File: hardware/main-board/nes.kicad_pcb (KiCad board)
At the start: 2 copper layers, 127 x 114.3 mm, 137 parts, among them J1 Power Jack, J2 Input Board, J3 Speaker, J4 Program, J5 NHD OLED Connector, J6 microSD Socket, Q1 S8050, Q2 S8050, Q3 S8050, SW1 NES Reset, SW2 ESP Reset, U1 R-78E5.0-0.5, U10 74HCT00, U11 PCA9564, U12 MCP7940N, U13 ESP-WROOM-32, U15 EClamp2410P, U2 R-78E3.3-0.5, U3 74LVC1404, U4 RP2A03, U5 74HCT138, U6 LM4889, U7 AS6C6264, U8 MCP40D17, U9 AT28C64B, Y1 21.5 MHz, Y2 32.768 kHz

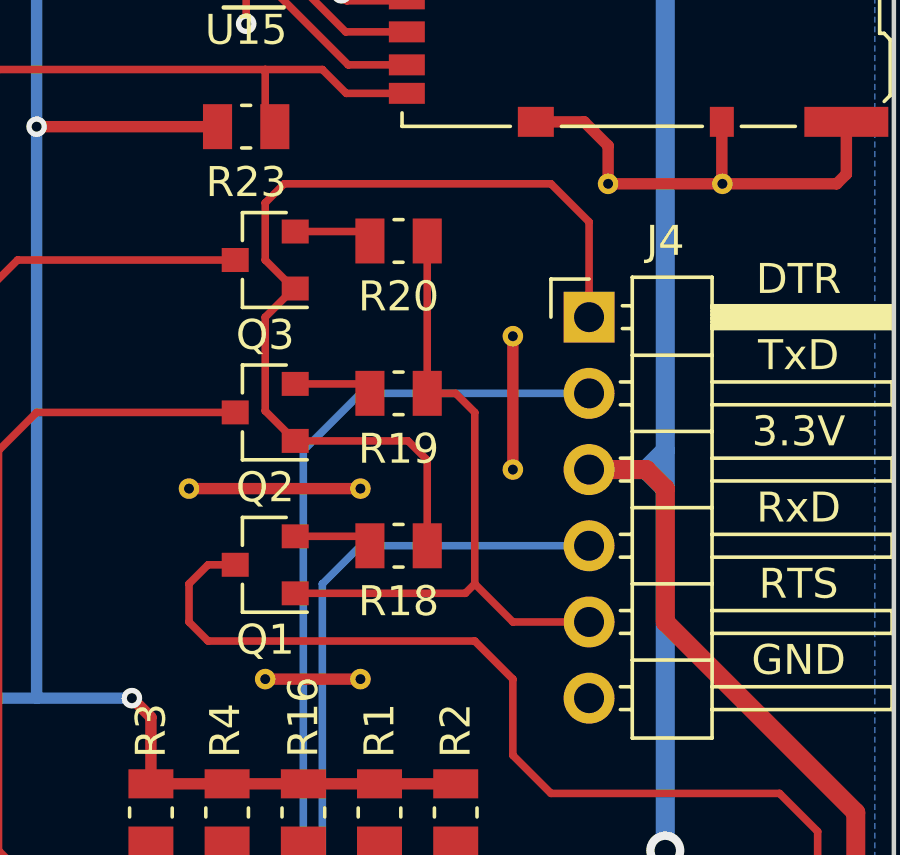
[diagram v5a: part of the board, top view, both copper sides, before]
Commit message: Create new component to fix Q1/Q2/Q3 pin mapping issues
Apparently the S8050 included in the KiCad library was for the TO-92
version of the part, for which the pin mapping was correct. The part
we're using is a SOT-23, more completely called SS8050, and has
different specifications. So fixing the issue meant creating a new
library symbol with the right pin assignments.

The PCB layout has also been updated to reflect this change.

Fixes #5
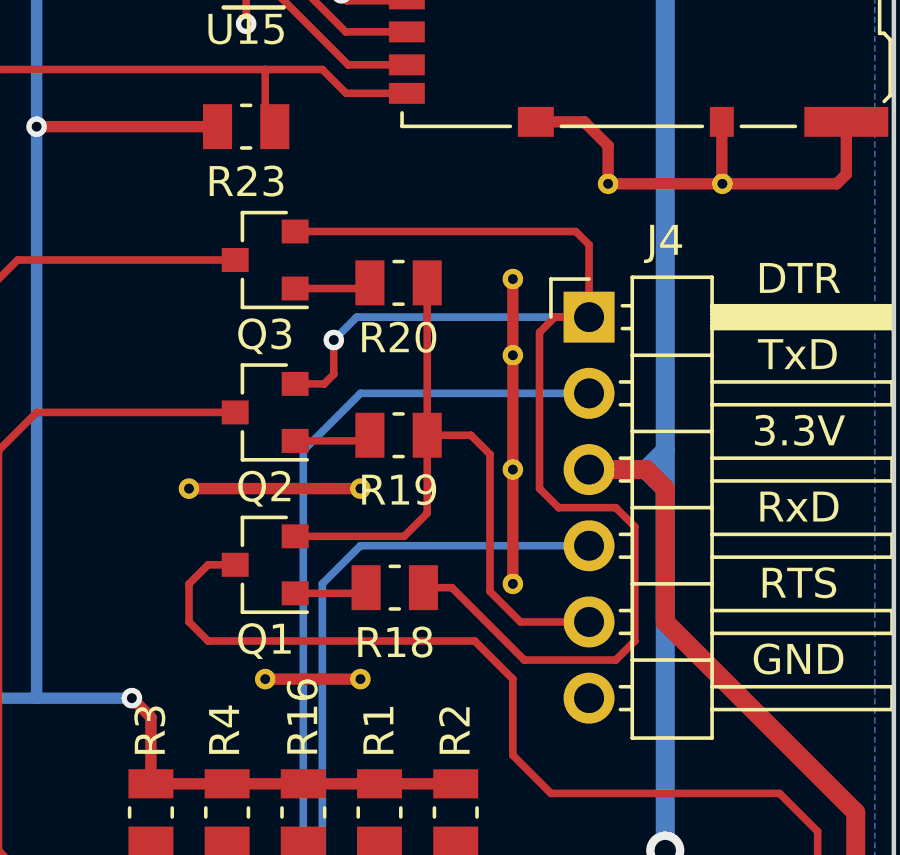
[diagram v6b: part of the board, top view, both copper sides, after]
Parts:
- added REF**: Via_27mill, lib_fp:Via_27mill, F.Cu at (174.0, 104.8)
- added REF**: Via_27mill, lib_fp:Via_27mill, F.Cu at (174.0, 97.2)
- Q1, Q2, Q3: value S8050 -> SS8050
- moved REF** 1.91 mm to (174.0, 94.6)
- moved R18 1.40 mm to (170.1, 104.9)
- moved R19 1.40 mm to (170.2, 99.8)
- moved R20 1.40 mm to (170.2, 94.7)
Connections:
- Q1 pad 1: /ESP32 Microcontroller/RTS -> Net-(Q1-Pad1)
- Q1 pad 2: Net-(Q1-Pad2) -> /ESP32 Microcontroller/RTS
- Q2 pad 1: /ESP32 Microcontroller/DTR -> Net-(Q2-Pad1)
- Q2 pad 2: Net-(Q2-Pad2) -> /ESP32 Microcontroller/DTR
- Q3 pad 1: /ESP32 Microcontroller/DTR -> Net-(Q3-Pad1)
- Q3 pad 2: Net-(Q3-Pad2) -> /ESP32 Microcontroller/DTR
- R18 pad 2: Net-(Q1-Pad2) -> Net-(Q1-Pad1)
- R19 pad 2: Net-(Q2-Pad2) -> Net-(Q2-Pad1)
- R20 pad 2: Net-(Q3-Pad2) -> Net-(Q3-Pad1)
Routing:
- net /ESP32 Microcontroller/DTR: track 31.8 -> 46.7 mm, vias 0 -> 1
- net GND: track 414.5 -> 420.3 mm
- net Net-(Q3-Pad1): track 0.00 -> 2.66 mm
- net Net-(Q3-Pad2): track 2.62 -> 0.00 mm
- net Net-(Q2-Pad2): track 2.62 -> 0.00 mm
- net Net-(Q1-Pad2): track 2.62 -> 0.00 mm
- net Net-(Q2-Pad1): track 0.00 -> 2.57 mm
- net Net-(Q1-Pad1): track 0.00 -> 2.44 mm

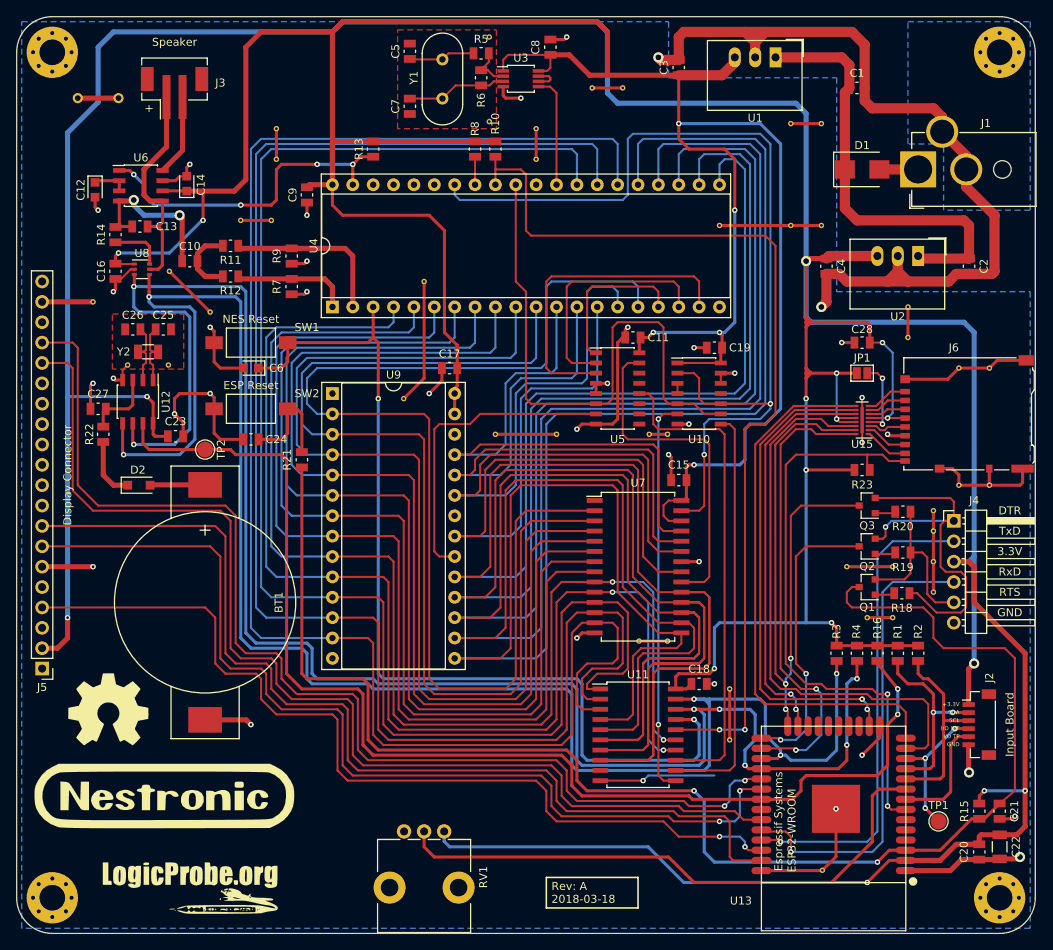
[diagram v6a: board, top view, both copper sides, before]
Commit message: Swap U11 from SOIC to TSSOP footprint
This was a trivial part change, with quite extensive trace routing
changes.

Fixes #2
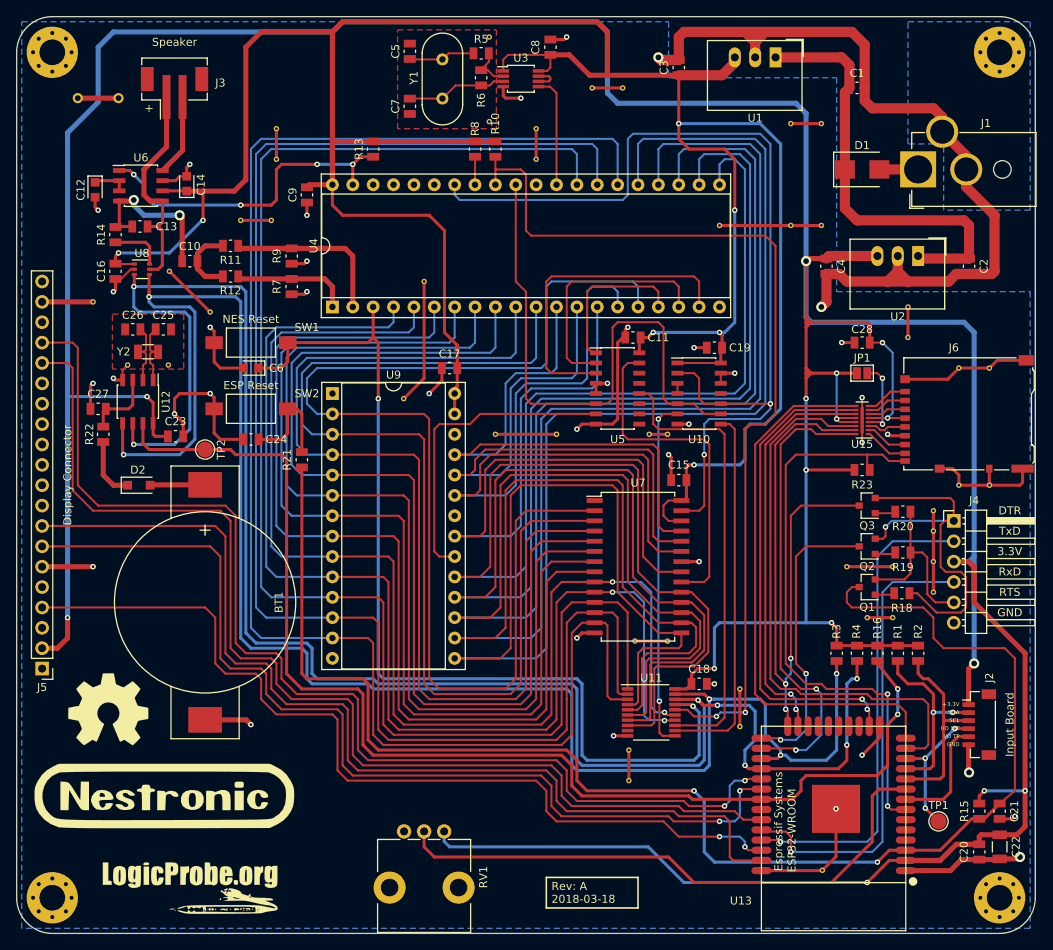
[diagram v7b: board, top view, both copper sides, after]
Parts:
- added REF**: Via_27mill, lib_fp:Via_27mill, F.Cu at (136.0, 124.5)
- added REF**: Via_27mill, lib_fp:Via_27mill, F.Cu at (136.0, 128.3)
- U11: footprint Package_SO:SOIC-20W_7.5x12.8mm_P1.27mm -> Package_SO:TSSOP-20_4.4x6.5mm_P0.65mm
- moved U11 3.25 mm to (138.8, 119.8)
- moved REF** 2.08 mm to (149.9, 121.5)
- moved REF** 1.27 mm to (149.9, 116.8)
- moved REF** 0.51 mm to (136.8, 110.9)
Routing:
- net /NES CPU/D7: track 219.8 -> 173.4 mm
- net /NES CPU/D6: track 222.0 -> 180.7 mm
- net /NES CPU/D5: track 224.2 -> 188.0 mm
- net GND: track 420.3 -> 410.2 mm
- net /NES CPU/D2: track 200.4 -> 194.6 mm
- net /NES CPU/~WR: track 49.5 -> 44.0 mm
- net /NES CPU/D1: track 195.4 -> 190.0 mm
- net /NES CPU/~RD: track 51.5 -> 46.5 mm
- net /NES CPU/D0: track 190.3 -> 185.3 mm
- net /NES CPU/D3: track 204.1 -> 199.4 mm
- net /NES CPU/D4: track 200.5 -> 196.0 mm
- net /NES CPU/Y3: track 61.0 -> 56.5 mm
- net /NES CPU/A0: track 150.5 -> 147.1 mm
- net /NES CPU/A1: track 151.8 -> 148.8 mm
- net +3V3: track 569.4 -> 566.9 mm
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
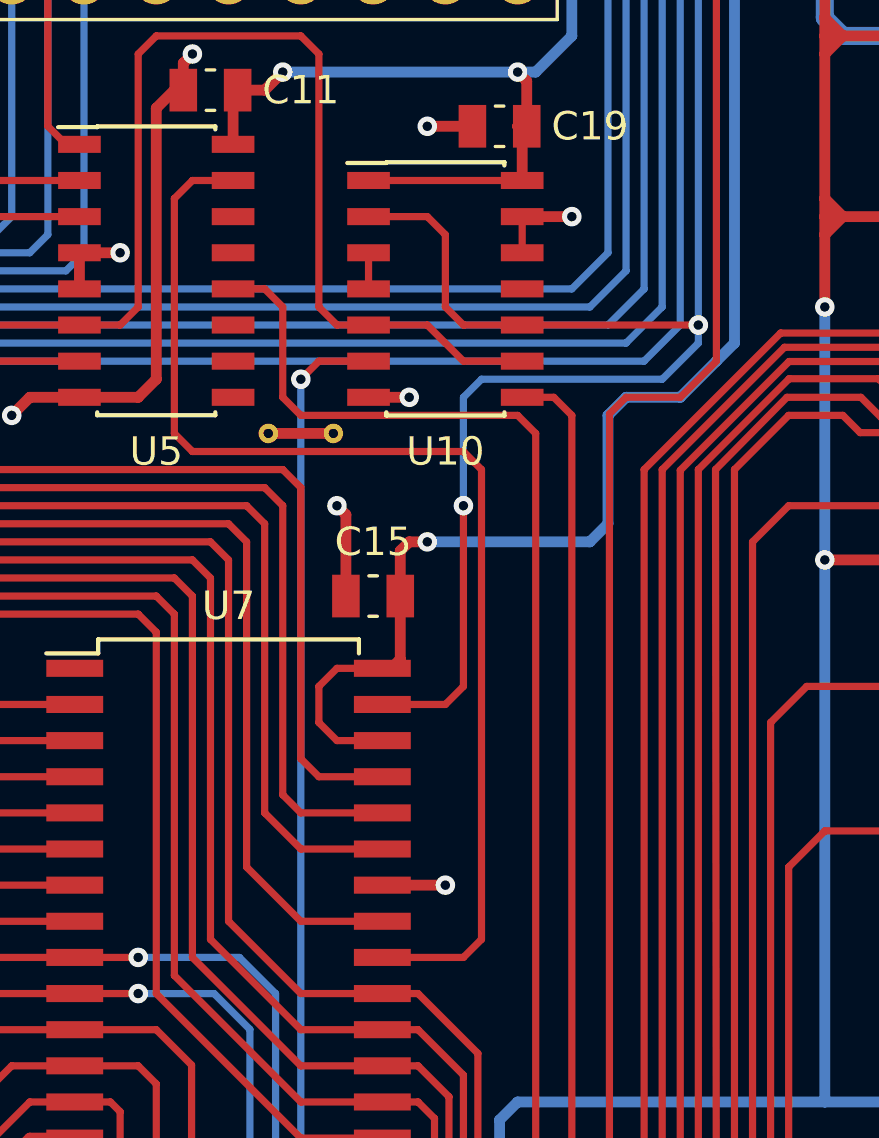
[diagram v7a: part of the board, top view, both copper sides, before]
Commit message: Change SRAM address decoding to mirror it onto address $C000
To support the NES APU's DMC feature, we need sample memory placed
around address $C000. Since we're only using a tiny portion of our RAM,
the easiest way is to mirror the RAM onto both $0000 and $C000.

This can be accomplished with a spare NAND gate already in our circuit,
and the secondary non-inverting chip enable line of the SRAM chip. The
idea is that if either Y0 or Y6 is low, then the output of the NAND gate
will be high, and thus select the chip.

Fixes #7
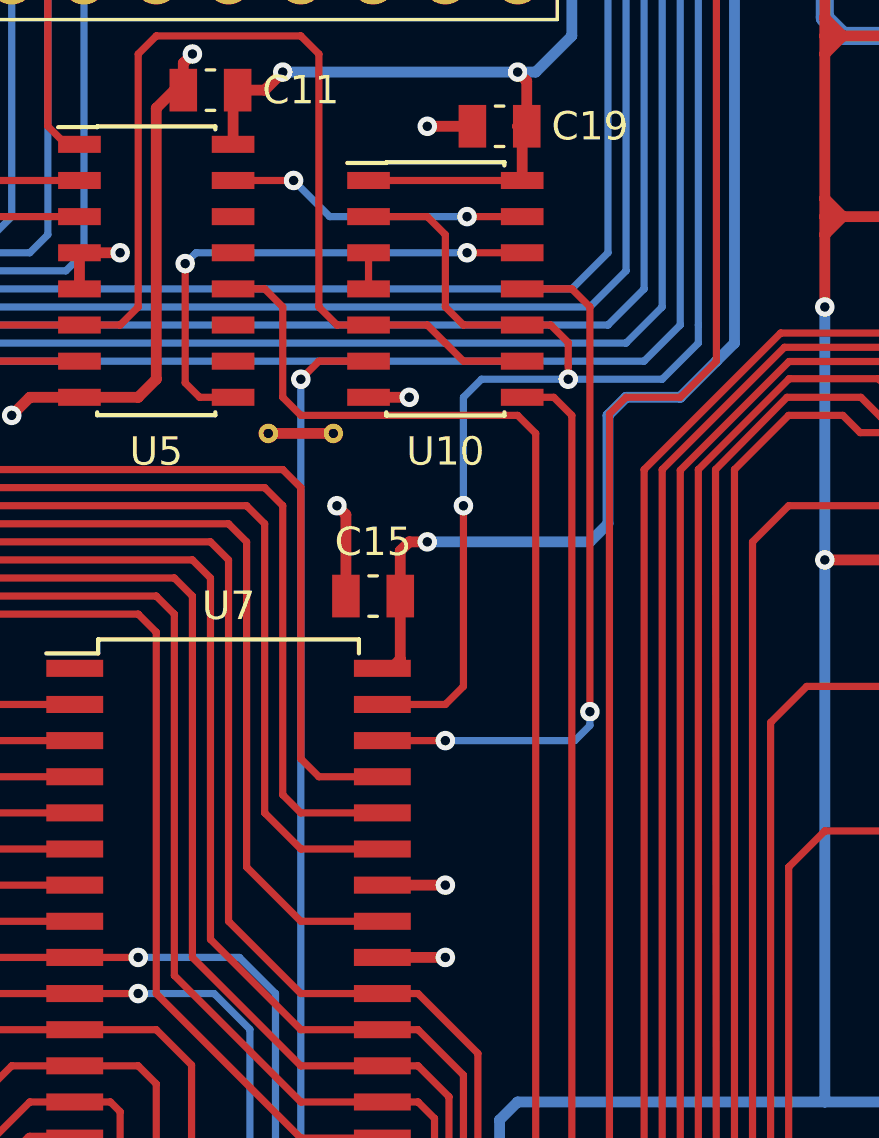
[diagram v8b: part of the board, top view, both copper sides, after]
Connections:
- U10 pad 12: GND -> /NES CPU/Y6
- U10 pad 13: GND -> /NES CPU/Y0
- U5 pad 9: Net-(U5-Pad9) -> /NES CPU/Y6
- U7 pad 20: /NES CPU/Y0 -> GND
- U7 pad 26: +5V -> Net-(U10-Pad11)
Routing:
- net /NES CPU/Y0: track 42.9 -> 10.7 mm, vias 0 -> 2
- net Net-(U10-Pad11): track 0.00 -> 24.9 mm, vias 0 -> 2
- net /NES CPU/Y6: track 0.00 -> 18.1 mm, vias 0 -> 2
- net +5V: track 361.3 -> 355.0 mm
- net /NES CPU/R~W: track 119.6 -> 116.6 mm
- net GND: track 410.2 -> 409.4 mm
